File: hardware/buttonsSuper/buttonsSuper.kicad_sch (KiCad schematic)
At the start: 15 parts, among them U1 SKRBAKE010, U2 SKRBAKE010, U3 SKRBAKE010, U4 SKRBAKE010, U5 SKRBAKE010

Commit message: Latest
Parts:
- removed C3: trill-flex-conector_10, consolizer:flex_short_10, symbol consolizer:trill-flex-conector_10
- removed U1 (x2), U2 (x2), U3 (x2), U4 (x2), U5 (x2): SKRBAKE010, JLCPCB_footprint:KEY-SMD_4P-L4.0-W4.8-P3.90-LS4.8, symbol JLCPCB_schematic:SKRBAKE010
- added C3: flex-conector_10, consolizer:flex_long_10, symbol consolizer:flex-conector_10
- added CIRCLE1, CROSS1, DOWN1, L1, LEFT1, R1, RIGHT1, SQUARE1, TRIANGLE1, UP1: K2-1187SQ-E4SW-06, JLCPCB_footprint:KEY-SMD_4P-L5.2-W5.2-P3.70-LS6.4, symbol JLCPCB_schematic:K2-1187SQ-E4SW-06
- C1, C2: value trill-flex-conector_10 -> flex-conector_10; footprint consolizer:flex_long_10 -> consolizer:flex_short_10
- C1: value trill-flex-conector_14 -> flex-conector_14
- C2: value trill-flex-conector_8_1 -> flex-conector_8_1
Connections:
- net Circle: now also C1.11, C3.4, CIRCLE1.1, CIRCLE1.2; no longer C1.4
- net GND: now also DOWN1.3, DOWN1.4, L1.3, L1.4, LEFT1.3, LEFT1.4, RIGHT1.3, RIGHT1.4, UP1.3, UP1.4
- net R1: now also C1.13, C3.2, R1.1, R1.2; no longer C1.2
- net Square: now also C1.14, C3.1, SQUARE1.1, SQUARE1.2; no longer C1.1
- net Triangle: now also C1.12, C3.3, TRIANGLE1.1, TRIANGLE1.2; no longer C1.3
- net cross: now also C1.10, C3.5, CROSS1.1, CROSS1.2; no longer C1.5
- net down: now also DOWN1.1, DOWN1.2
- net five: now also C1.1, C2.7; no longer C1.14, C2.2
- net four: now also C1.2, C2.6; no longer C1.13, C2.3
- net gnd: now also C2.1, C2.2, C3.6, CIRCLE1.3, CIRCLE1.4, CROSS1.3, CROSS1.4, R1.3, R1.4, SQUARE1.3, SQUARE1.4, TRIANGLE1.3, TRIANGLE1.4; no longer C2.7, C2.8
- net l1: now also L1.1, L1.2
- net left: now also LEFT1.1, LEFT1.2
- net one: now also C1.5, C2.3; no longer C1.10, C2.6
- net right: now also RIGHT1.1, RIGHT1.2
- net three: now also C1.3, C2.5; no longer C1.12, C2.4
- net tw: now also C1.4, C2.4; no longer C1.11, C2.5
- net up: now also UP1.1, UP1.2
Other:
- note added: "LEFT"
- note added: "RIGHT"

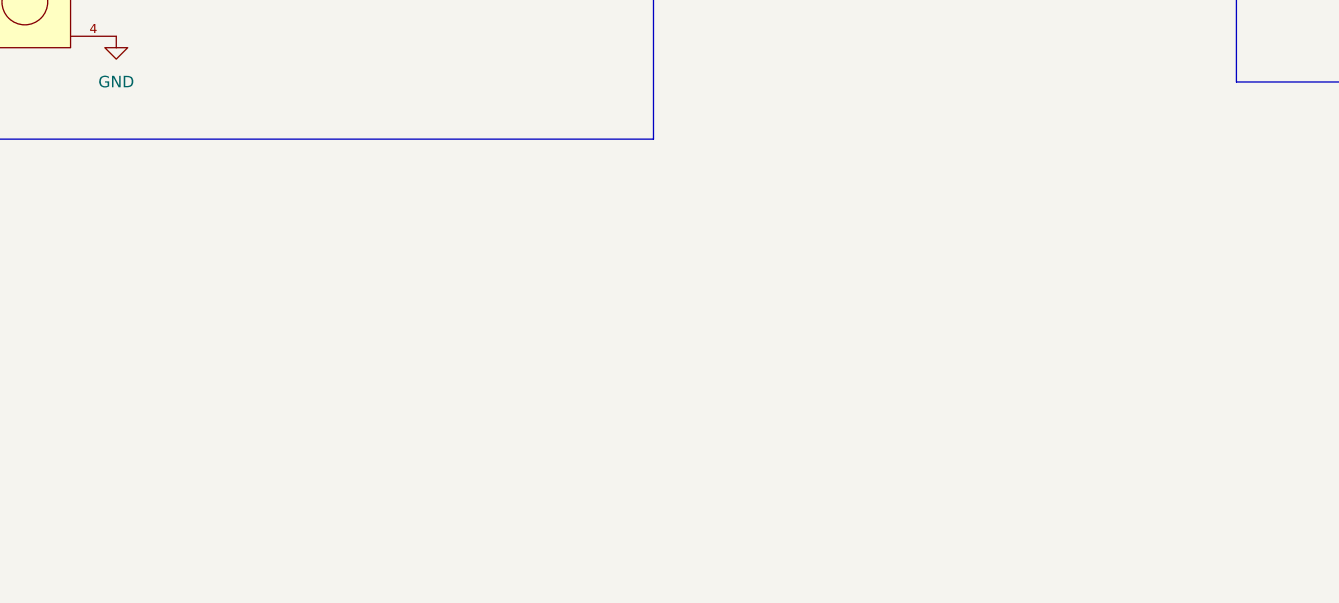
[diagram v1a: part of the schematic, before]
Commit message: Added analog stick
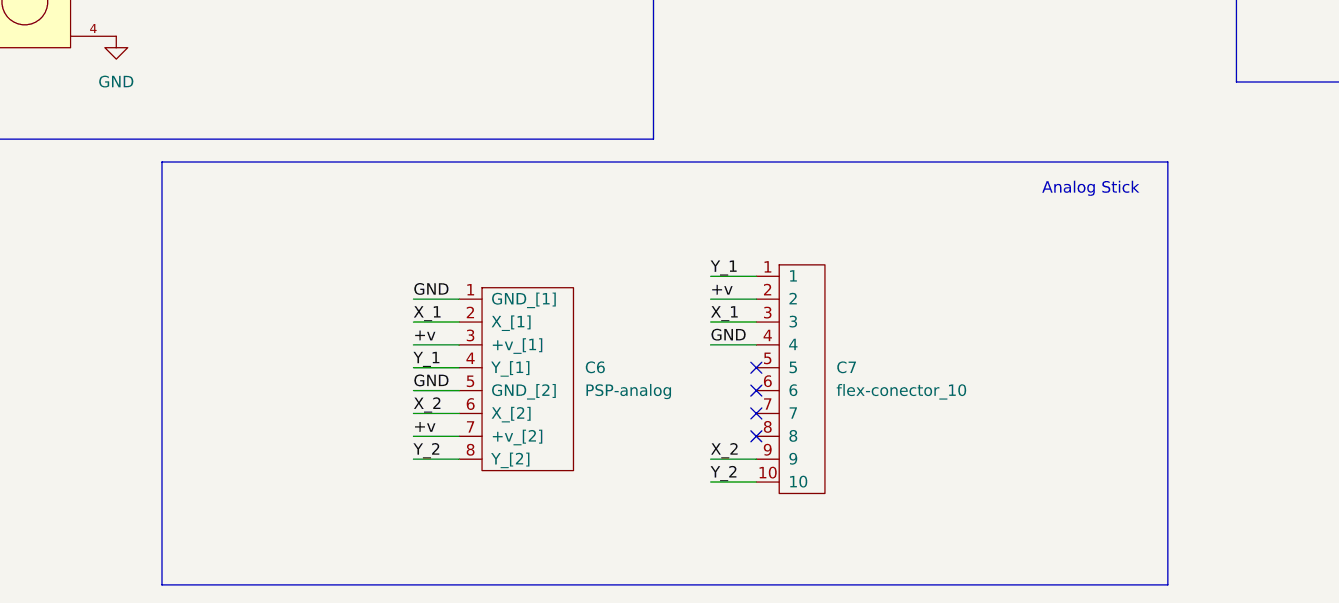
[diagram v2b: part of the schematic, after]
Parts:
- added C6: PSP-analog, consolizer:PSP-analog, symbol consolizer:PSP-analog
- added C7: flex-conector_10, consolizer:flex_long_10, symbol consolizer:flex-conector_10
- CIRCLE1, CROSS1, DOWN1, L1, LEFT1, R1, RIGHT1, SQUARE1, TRIANGLE1, UP1: footprint JLCPCB_footprint:KEY-SMD_4P-L5.2-W5.2-P3.70-LS6.4 -> JLCPCB_footprint:KEY-SMD_4P-L5.2-W5.2-P3.70-LS6.4_1
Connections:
- net GND: now also C6.1 (GND_[1]), C6.5 (GND_[2]), C7.4
- new net +v: C6.3 (+v_[1]), C6.7 (+v_[2]), C7.2
- new net X_1: C6.2 (X_[1]), C7.3
- new net X_2: C6.6 (X_[2]), C7.9
- new net Y_1: C6.4 (Y_[1]), C7.1
- new net Y_2: C6.8 (Y_[2]), C7.10
- no-connect marks 5 -> 9
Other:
- note added: "Analog Stick"
